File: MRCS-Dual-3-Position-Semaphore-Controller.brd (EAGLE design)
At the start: 99.8 x 68.8 mm, 24 parts, among them J1 9 VDC, M1 SMALL_SERVO, M2 SMALL_SERVO

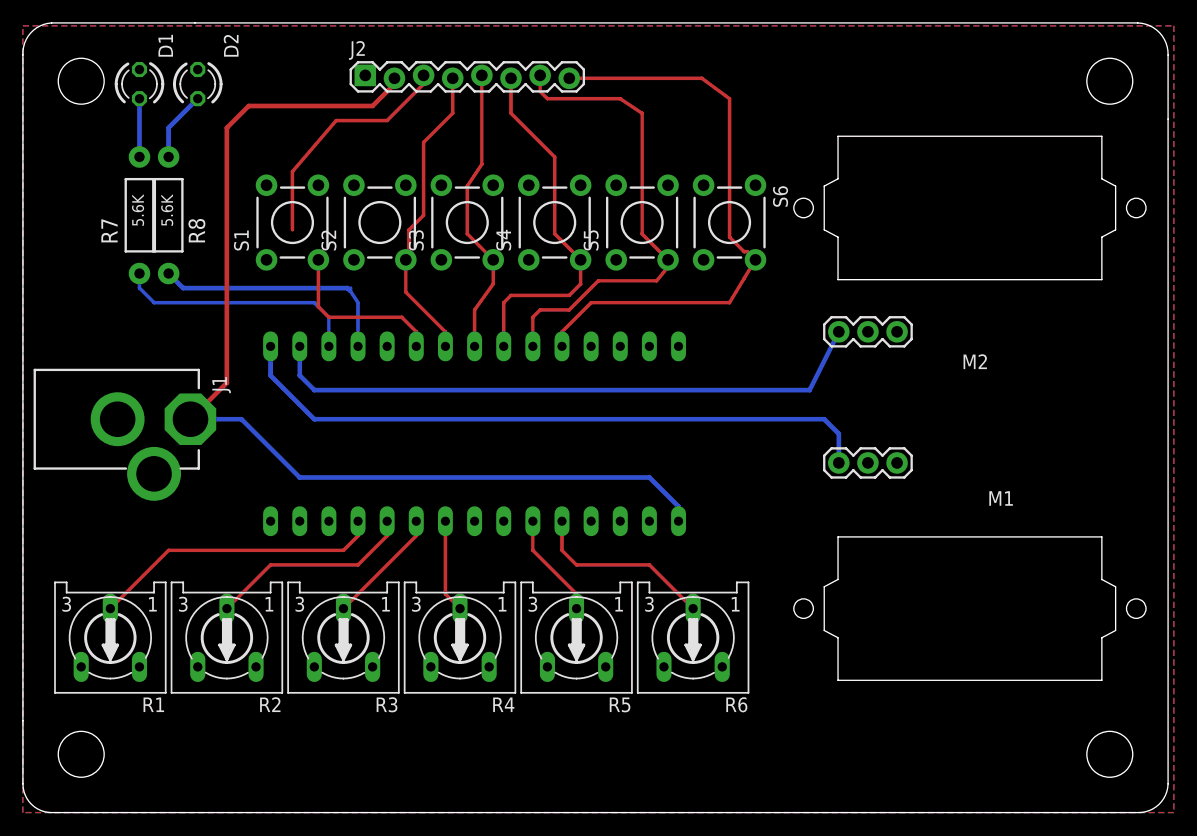
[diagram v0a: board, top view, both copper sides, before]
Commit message: Version 1.o documentation package
includes documentation, brd, sch, zip, and sketch
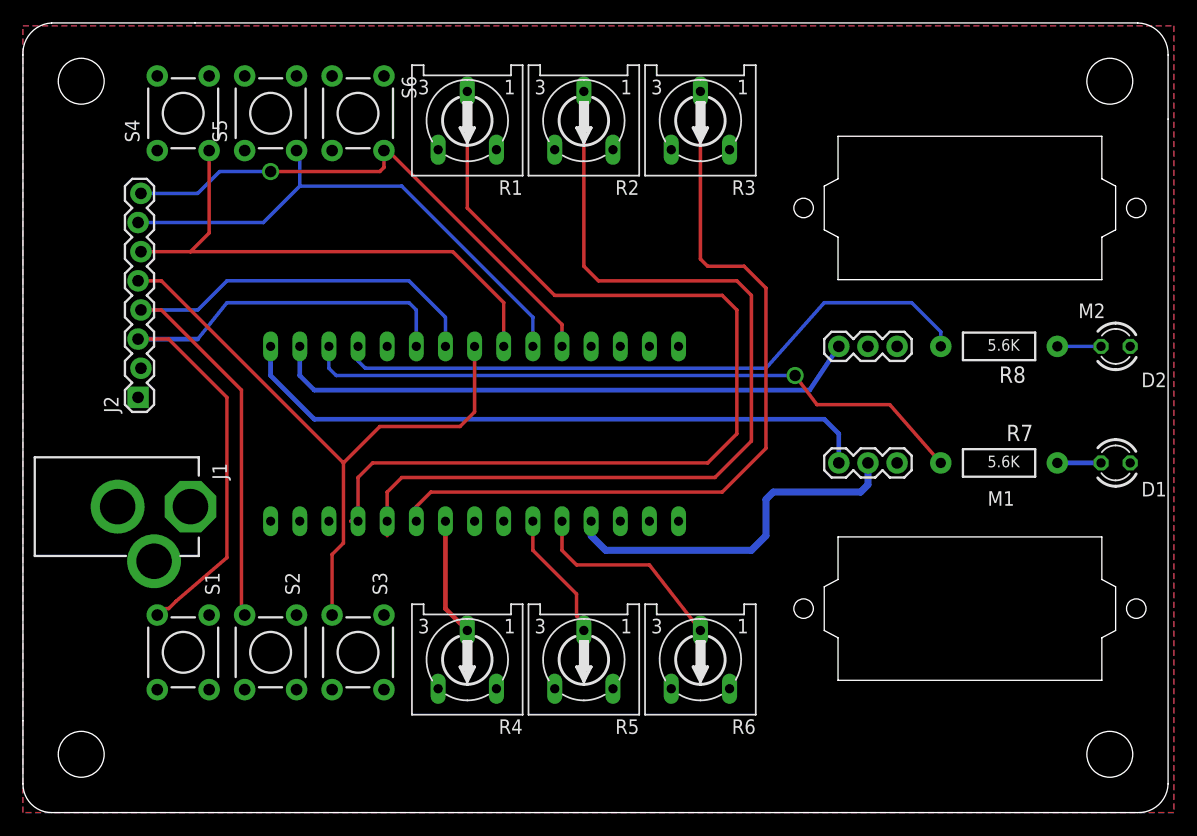
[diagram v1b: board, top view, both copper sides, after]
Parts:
- added U$3: (no value), MRCSLogoBtm:MRCSLOGOBTM
- added U$5: (no value), MRCS-prop65warningBtm:CA-PROP65WARNING
- J1: value 9 VDC -> 5 VDC
- J2: value (none) -> Input
- moved D1 91.3 mm to (95.2, 30.5), turned to 180 degrees
- moved D2 83.2 mm to (95.2, 40.6), turned to 180 degrees
- moved R7 78.0 mm to (85.1, 30.5), turned to 0 degrees
- moved R8 73.3 mm to (85.1, 40.6), turned to 0 degrees
- moved R1 54.8 mm to (38.7, 60.3)
- moved R2 54.8 mm to (48.9, 60.3)
- moved R3 54.8 mm to (59.1, 60.3)
- moved S1 38.7 mm to (14.0, 14.0), turned to 270 degrees
- moved S2 38.7 mm to (21.6, 14.0), turned to 270 degrees
- moved S3 38.7 mm to (29.2, 14.0), turned to 270 degrees
- moved J2 34.2 mm to (10.2, 36.2), turned to 90 degrees
- moved S5 33.8 mm to (21.6, 61.0)
- moved S4 33.8 mm to (14.0, 61.0)
- moved S6 33.8 mm to (29.2, 61.0)
- moved J1 7.62 mm to (11.4, 26.7)
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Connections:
- net A4 renamed A6
- net A5 renamed A7
- net N$10 renamed D4
- net N$11 renamed D5
- net N$12 renamed D6
- net N$13 renamed D7
- net N$2 renamed D10
- net N$3 renamed D11
- net N$5 renamed D12
- net N$6 renamed D2
- net N$9 renamed D3
- removed net RAW: J1.1, J2.2, NANO.RAW
- net 5V: now also J1.1, J2.2
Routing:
- net RAW: track 90.4 -> 0.00 mm
- net A1: track 17.9 -> 81.0 mm
- net A0: track 25.5 -> 87.4 mm
- net A2: track 10.3 -> 69.2 mm
- net D10: track 21.4 -> 59.1 mm, vias 0 -> 1
- net D6: track 26.5 -> 63.5 mm
- net N$17: track 21.7 -> 57.2 mm
- net 5V: track 0.00 -> 32.1 mm
- net D5: track 25.5 -> 57.1 mm
- net D7: track 35.4 -> 61.0 mm
- net D4: track 31.6 -> 46.8 mm
- net D3: track 41.7 -> 46.2 mm
- net D2: track 51.0 -> 47.3 mm, vias 0 -> 1
- net A6: track 9.20 -> 12.0 mm
- net N$8: track 6.13 -> 3.81 mm
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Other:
- board text added: "BRN ORN"
- board text added: "GN2 YL2 RD2 GR1 YL1 RD1 +5V GND"
- board text added: "GRN"
- board text added: "RED"
- board text added: "V1.0 20210103"
- board text added: "YEL"
- board text removed: "BROWN ORANGE"
- board text removed: "GND +9V GR2 YL2 RD2 GR1 YL1 RD1"
- board text removed: "V1.0 20201224"
